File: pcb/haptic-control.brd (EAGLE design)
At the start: 40 x 160 mm, 71 parts, among them J1 PAD1X3_5MM-2P, J2 PAD1X3_5MM-2P, M1 SPH0641LM4H-1, U1 CC2642R, U10 FS8205, U2 SST26VF064B, U3 ICM20948, U4 74LVC1G17, U5 MCP1700T-1802TT, U6 PCA9306-DCU, U7 MTCH6301, U8 BQ51050B, U9 FS312F-G, X1 48MHz, X2 32.768kHz

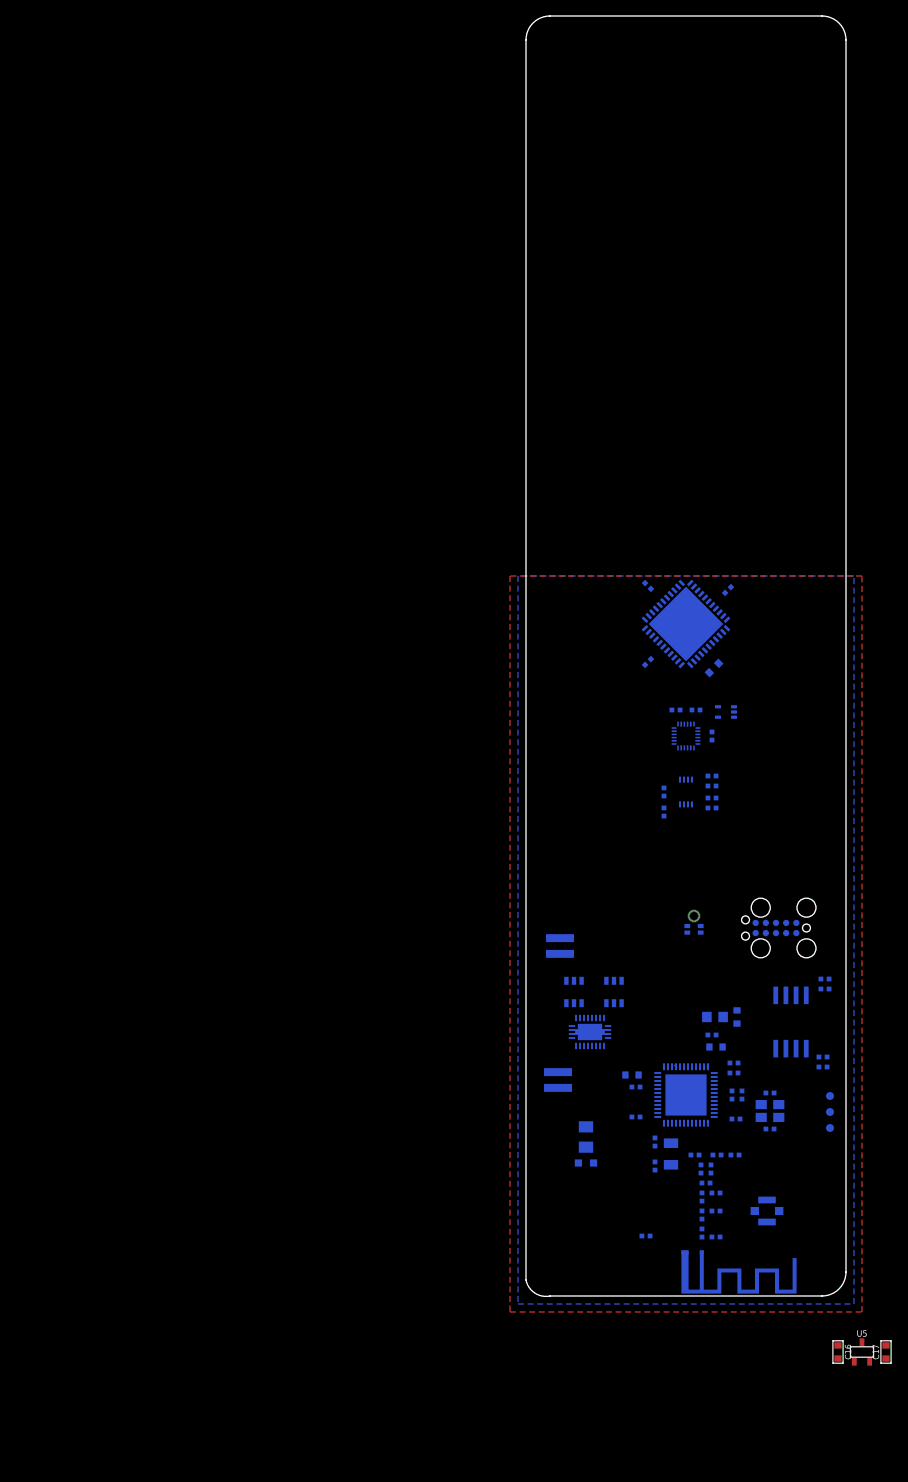
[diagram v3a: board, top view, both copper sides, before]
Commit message: added LRA drivers, added FSRs
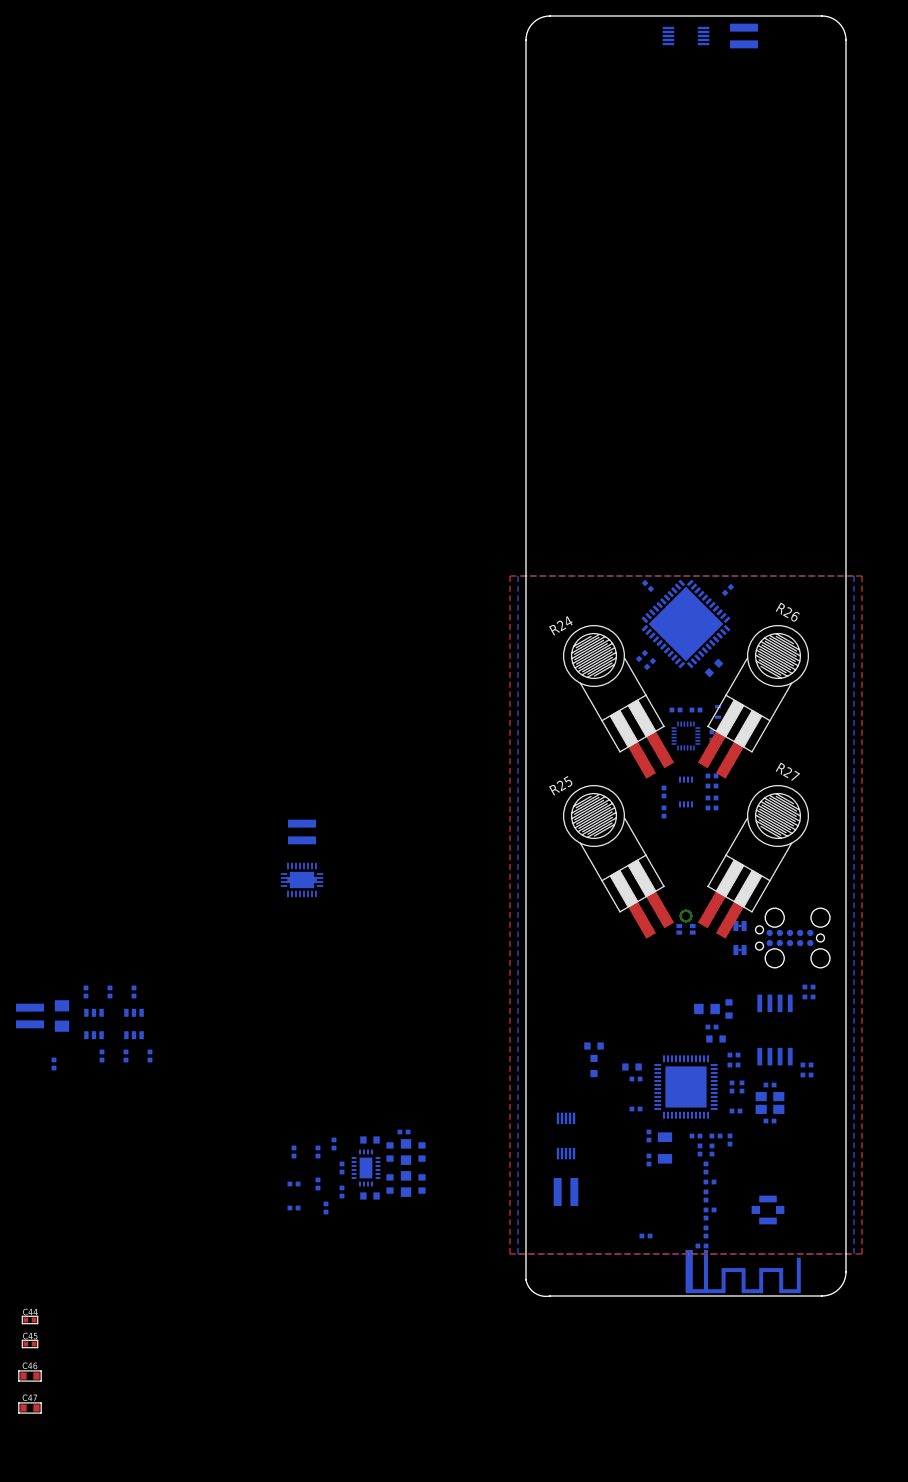
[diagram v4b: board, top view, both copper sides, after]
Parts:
- removed J1, J2: PAD1X3_5MM-2P, Connectors > Other:PAD1X3_5MM-2P
- removed TP1, TP2, TP3: TEST_POINT, Utility > Board:TEST_POINT
- added C36, C44, C45: 100n, Passive Components > Capacitors > Multilayer Ceramic Capacitors MLCC:_0402
- added C37, C38, C46, C47: 1u, Passive Components > Capacitors > Multilayer Ceramic Capacitors MLCC:0603_WAVE
- added C39, C42: 4u7, Passive Components > Capacitors > Multilayer Ceramic Capacitors MLCC:0603_WAVE
- added C40, C41: 470p, Passive Components > Capacitors > Multilayer Ceramic Capacitors MLCC:_0402
- added C43: 100u, Passive Components > Capacitors > Multilayer Ceramic Capacitors MLCC:_1206
- added JP1, JP2: JUMPER-SMT_2_NC_TRACE_SILK, Utility > Board:SMT-JUMPER_2_NC_TRACE_SILK
- added L7, L8: 1u, Passive Components > Inductors, Chokes & Coils:_0805
- added P1, P2, P3, P4: 2P-PAD_1X3.5, Connectors > Other:PAD1X3_5MM-2P
- added R10, R13, R16, R17, R20, R21: 100k, Passive Components > Resistors > Chip Resistors:_0402
- added R11: 10M, Passive Components > Resistors > Chip Resistors:_0402
- added R12: 100, Passive Components > Resistors > Chip Resistors:_0402
- added R14: 47k, Passive Components > Resistors > Chip Resistors:_0402
- added R15: 1k, Passive Components > Resistors > Chip Resistors:_0402
- added R18: 309k, Passive Components > Resistors > Chip Resistors:_0402
- added R19: 71.5k, Passive Components > Resistors > Chip Resistors:_0402
- added R22: 301k, Passive Components > Resistors > Chip Resistors:_0402
- added R23: 158k, Passive Components > Resistors > Chip Resistors:_0402
- added R24, R25, R26, R27: FSR400-SHORT-TAIL, Interlink:FSR400-SHORT-TAIL
- added U$1, U$2: (no value), Eletromechanical > LRAs:G0825001
- added U11: MIC23159, Microchip:VQFN20
- added U12: DRV2605L, Texas Instruments:VSSOP10
- C16, C17: value 1u -> 4u7
- C27: value 100u -> 22u; device Passive Components > Capacitors > Multilayer Ceramic Capacitors MLCC:_1206 -> Passive Components > Capacitors > Multilayer Ceramic Capacitors MLCC:0603_WAVE
- C33: device Passive Components > Capacitors > Multilayer Ceramic Capacitors MLCC:_0402 -> Passive Components > Capacitors > Multilayer Ceramic Capacitors MLCC:_0402_SEL
- C34: value DNP -> 470p
- R8, R9: value 200k -> 4k7
- U5: value MCP1700T-1802TT -> DRV2605L; device Power > LDO Voltage Regulators:SOT-23 -> Texas Instruments:VSSOP10
- moved C34 80.5 mm to (-52.0, 38.0), turned to 270 degrees
- moved C17 67.4 mm to (-19.5, 12.5), flipped to the bottom, turned to 0 degrees
- moved C16 64.2 mm to (-19.5, 19.5), flipped to the bottom, turned to 0 degrees
- moved U10 60.1 mm to (-49.0, 34.0)
- moved U9 60.1 mm to (-54.0, 34.0)
- moved U5 45.8 mm to (5.00, 20.0), flipped to the bottom, turned to 270 degrees
- moved U8 40.7 mm to (-28.0, 52.0)
- moved L2 12.2 mm to (8.50, 28.8), turned to 270 degrees
- moved C27 11.4 mm to (8.50, 31.2), turned to 0 degrees
- moved C28 2.38 mm to (21.2, 20.0)
- moved C29 2.38 mm to (23.2, 18.2)
- moved L3 2.38 mm to (23.8, 20.0)
- moved L4 2.38 mm to (21.8, 18.2)
- moved C15 2.24 mm to (35.4, 37.4)
- moved R2 2.24 mm to (35.1, 28.9)
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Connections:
- new net 1V8_PG: R21.1, U11.12
- new net 3V3_PG: R17.1, U11.15
- new net GBAT: C36.2, P1.2, R11.2, U10.3, U9.6
- new net LRA_EN: U12.5, U5.5
- new net MPU_PWR: R20.1, U11.9
- new net N$12: C33.1, L6.1
- new net N$13: C32.1, C33.3
- new net N$21: U10.4, U9.1
- new net N$22: U10.6, U9.3
- new net N$23: C36.1, R12.1, U9.5
- new net N$24: R15.2, U9.2
- new net N$25: R18.1, R19.2, U11.16
- new net N$26: R16.1, U11.18
- new net N$27: P3.1, U5.7
- new net N$28: L7.2, U11.3
- new net N$29: C40.1, U11.14
- new net N$30: L8.2, U11.4
- new net N$31: C41.1, U11.13
- new net N$32: R22.2, R23.1, U11.11
- new net N$33: P3.2, U5.9
- new net N$34: P4.1, U12.7
- new net N$35: P4.2, U12.9
- new net N$36: C46.P$1, U5.1
- new net N$37: C47.P$1, U12.1
- new net VBAT: C16.P$1, C17.P$1, C37.P$1, C38.P$1, C43.1, C44.1, C45.1, P1.1, R12.2, R13.2, R16.2, R20.2, U11.1, U11.20, U11.6, U11.7, U12.10, U12.6, U5.10, U5.6
- new net VBAT_SNS: C34.1, R13.1, R14.2
- net 1.8V: now also C18.1, C42.P$1, L8.1, R22.1, U11.10, U3.13; no longer C17.P$1, U5.2
- net 3.3V: now also C27.P$1, C39.P$1, L7.1, R10.2, R17.2, R18.2, R21.2, U11.17; no longer C16.P$1, C18.1, C27.1, U3.13, U5.3
- net DBG_RX: now also JP2.1; no longer TP2.1, U1.40
- net DBG_TX: now also JP1.1; no longer TP1.1, U1.41
- net FLASH_CS: no longer U1.43
- net FLASH_MISO: no longer U1.28
- net FLASH_MOSI: no longer U1.29
- net GND: now also C27.P$2, C34.2, C37.P$2, C38.P$2, C39.P$2, C40.2, C41.2, C42.P$2, C43.2, C44.2, C45.2, C46.P$2, C47.P$2, R11.1, R14.1, R15.1, R19.1, R23.2, U10.1, U11.19, U11.2, U11.21, U11.5, U11.8, U12.4, U12.8, U5.4, U5.8; no longer C27.2, TP3.1, U5.1
- net I2S_CLK: no longer U1.31
- net I2S_DATIN: no longer U1.14
- net JTAG_TDI/FLASH_MOSI: no longer U1.27
- net JTAG_TDO: no longer U1.26
- net MPU_INT: no longer U1.8
- net N$18: now also A1.P$3; no longer C32.1
- net N$19: now also JP2.2, TC1.5; no longer C33.1, C34.2, L6.1
- net N$20: now also JP1.2, TC1.7; no longer A1.P$3, C34.1
- net SCL: now also U12.2, U5.2; no longer U1.6
- net SDA: now also U12.3, U5.3; no longer U1.5
- net TC_!RESET: now also R10.1

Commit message: TODO: qi, mcu connect
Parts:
- added C48, C49, C50, C51: 470p, Passive Components > Capacitors > Multilayer Ceramic Capacitors MLCC:_0402
- added F1: 500mA, PTC Fuses:0805
- added R28, R29, R30, R31: 3.4k, Passive Components > Resistors > Chip Resistors:_0402
- R14: value 47k -> 49.9k
- moved C47 186.5 mm to (11.2, 157.5), flipped to the bottom, turned to 90 degrees
- moved C45 182.0 mm to (20.5, 156.2), flipped to the bottom, turned to 180 degrees
- moved C46 75.3 mm to (3.25, 27.5), flipped to the bottom, turned to 180 degrees
- moved C44 67.8 mm to (2.00, 19.5), flipped to the bottom, turned to 270 degrees
- moved C34 66.7 mm to (14.2, 46.0), turned to 90 degrees
- moved P2 46.7 mm to (-20.0, 12.0)
- moved U8 46.7 mm to (-20.0, 6.00)
- moved R16 44.3 mm to (-19.5, 55.0), turned to 180 degrees
- moved C43 42.0 mm to (-16.8, 27.2), turned to 180 degrees
- moved R14 41.2 mm to (-14.0, 34.0)
- moved P1 40.6 mm to (-22.0, 28.0)
- moved R17 37.9 mm to (-23.8, 51.9), turned to 0 degrees
- moved U9 37.0 mm to (-17.0, 33.0)
- moved C22 36.8 mm to (20.0, 44.0)
- moved R19 36.8 mm to (-23.8, 54.4), turned to 180 degrees
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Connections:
- net JTAG_TDI/FLASH_MOSI renamed FLASH_SCK
- new net FSR_CH_N: C49.1, R25.2, R29.2
- new net FSR_CH_P: C48.1, R24.2, R28.2
- new net FSR_VOL_N: C51.1, R27.2, R30.2
- new net FSR_VOL_P: C50.1, R26.2, R31.2
- new net N$38: F1.1, P1.1
- net 3.3V: now also R24.1, R25.1, R26.1, R27.1
- net GND: now also C48.2, C49.2, C50.2, C51.2, R28.1, R29.1, R30.1, R31.1
- net JTAG_TDI: now also U1.27
- net JTAG_TDO: now also U1.26
- net SCL: now also R3.1
- net SDA: no longer R3.1
- net VBAT: now also F1.2; no longer P1.1
